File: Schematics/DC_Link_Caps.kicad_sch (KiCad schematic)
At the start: 15 parts

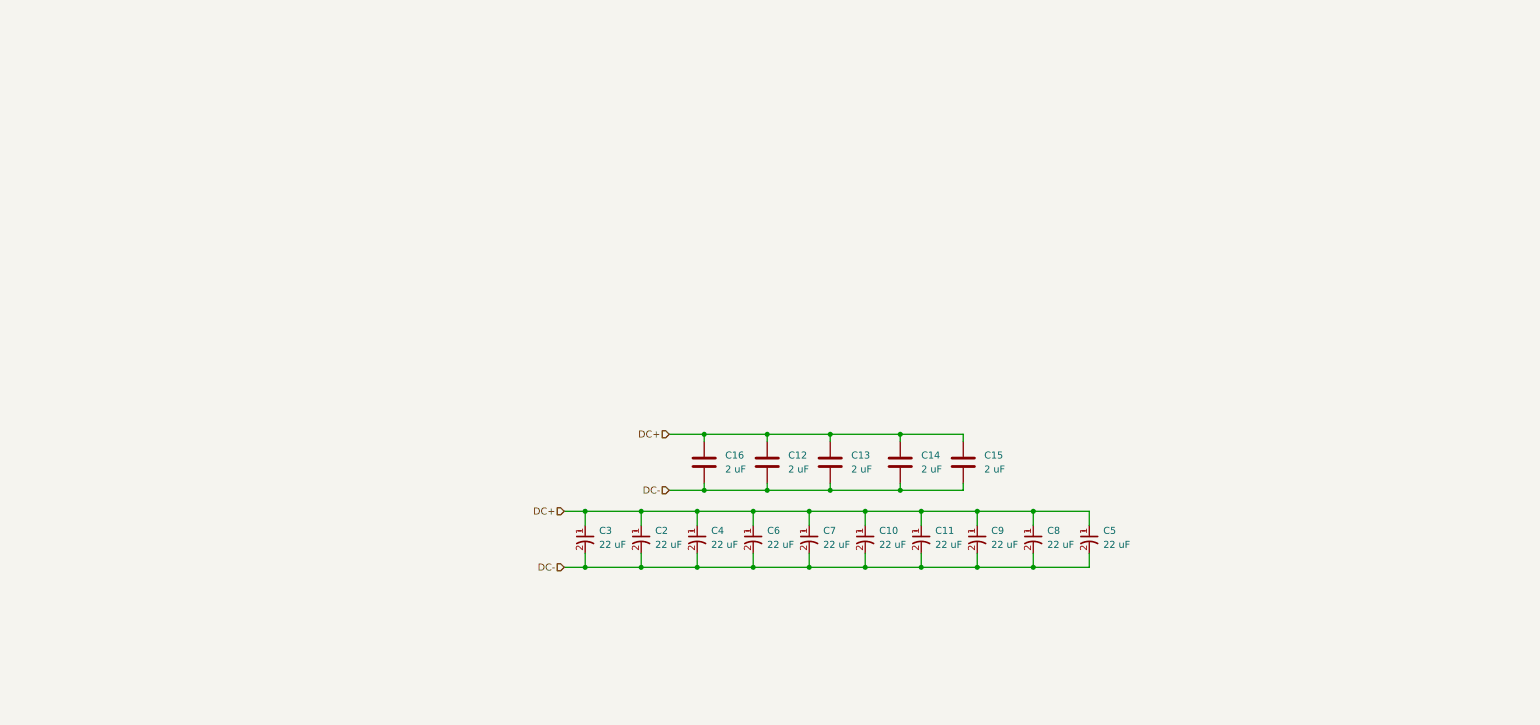
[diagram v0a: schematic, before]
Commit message: [SiC Inverter WIP]
- Deleted backup files
- changed symbol and footprint lib locations
- added text discription explaining the DC link sub sheet and emi  input
  filter subsheet
- Added Vin+,- Black and Red connector
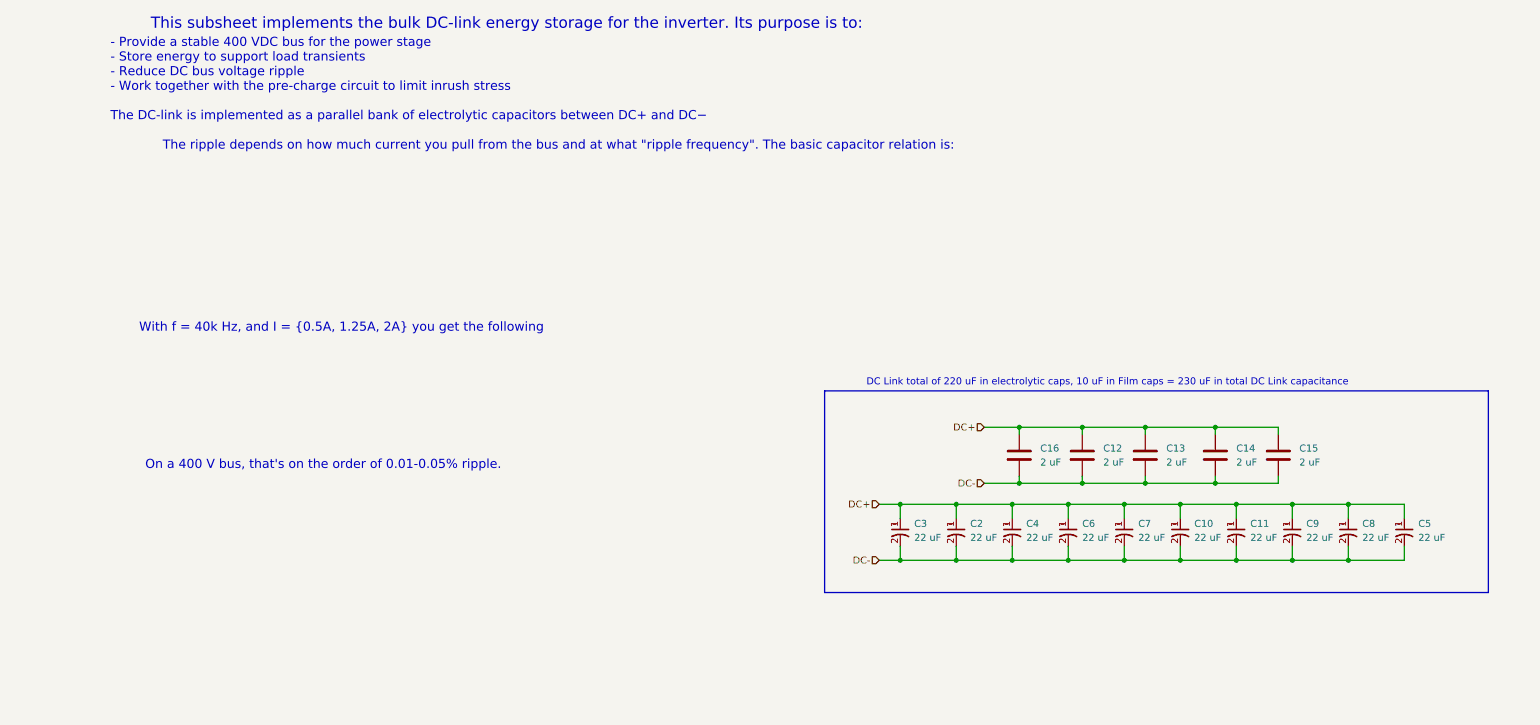
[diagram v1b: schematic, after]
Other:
- note added: "- Provide a stable 400 VDC bus for the power stage - Store energy to support load transients - Reduce DC bus voltage ripple - Work together with the pre‑charge circuit to limit inrush stress The DC‑link is implemented as a parallel bank of electrolytic capacitors between DC+ and DC−"
- note added: "DC Link total of 220 uF in electrolytic caps, 10 uF in Film caps = 230 uF in total DC Link capacitance"
- note added: "On a 400 V bus, that's on the order of 0.01-0.05% ripple."
- note added: "The ripple depends on how much current you pull from the bus and at what "ripple frequency". The basic capacitor relation is:"
- note added: "This subsheet implements the bulk DC‑link energy storage for the inverter. Its purpose is to:"
- note added: "With f = 40k Hz, and I = {0.5A, 1.25A, 2A} you get the following"
- moved on the sheet: C10, C11, C12, C13, C14, C15, C16, C2, C3, C4, C5, C6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

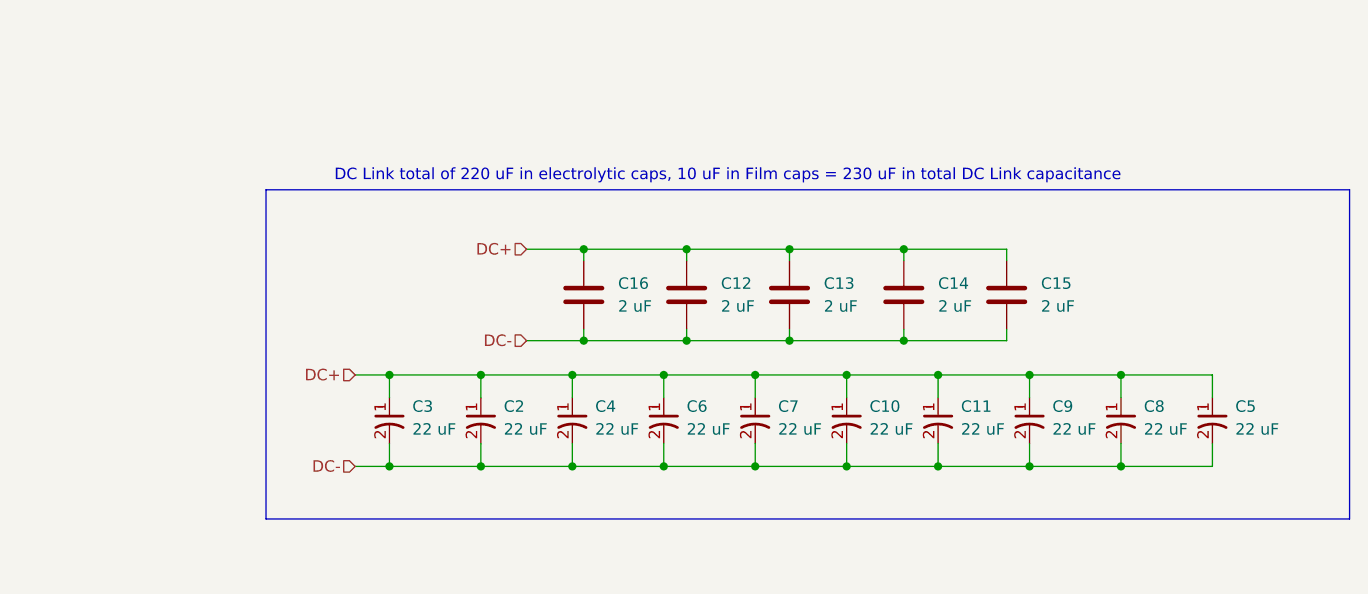
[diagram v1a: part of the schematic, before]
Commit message: [WIP - SIC Inverter]
- Added 3d models for 3 parts
- Added 3 new footprints for the 3 added parts
- Changed footprint 23AH8785 and 86 Black and Red
- Finished WIP with EMI, Input Protection, and Precharge
- Added datasheet
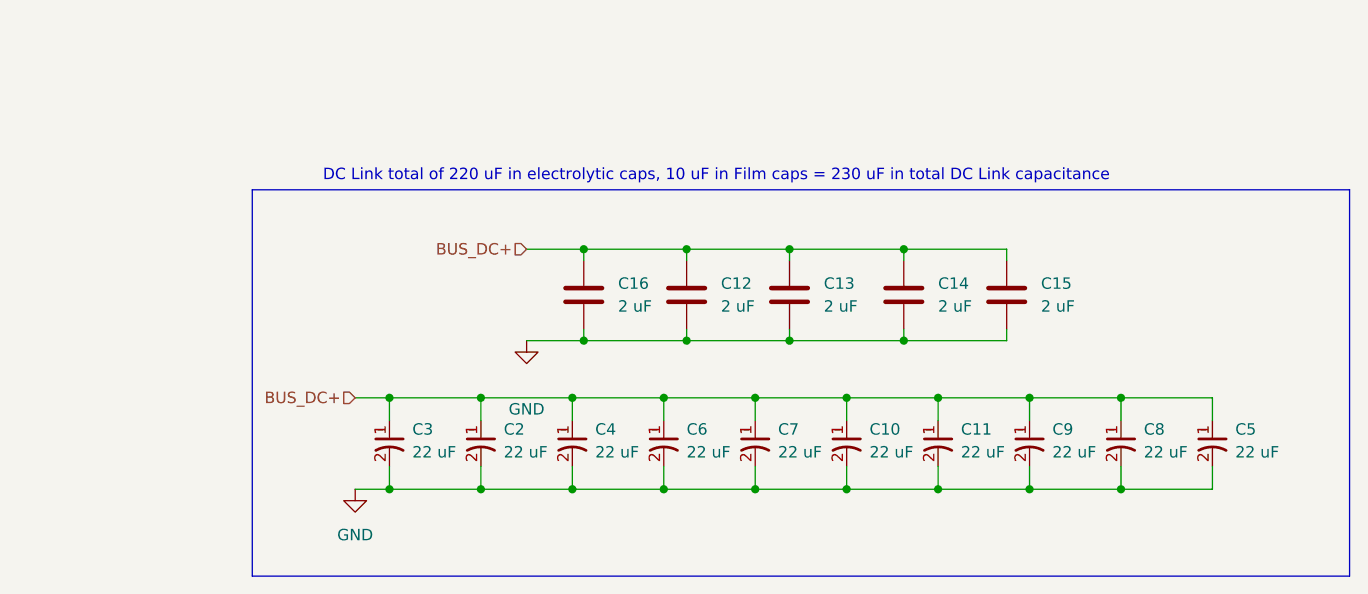
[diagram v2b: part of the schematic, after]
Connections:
- net DC+ renamed BUS_DC+
- net DC- renamed GND
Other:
- moved on the sheet: C10, C11, C2, C3, C4, C5, C6, C7, C8, C9

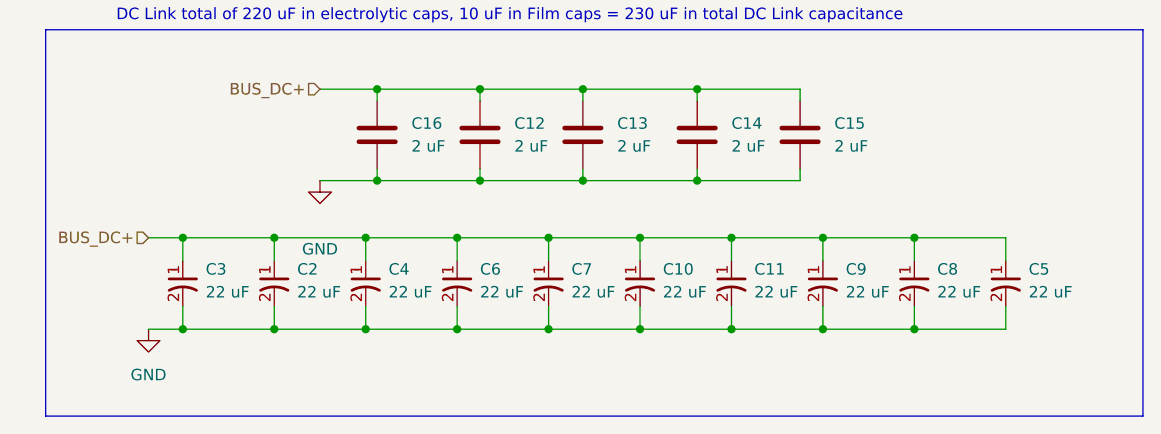
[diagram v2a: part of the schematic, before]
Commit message: [WIP Full Bridge Leg A High Side]
- Changed Footprint for Black and Red connectors to THP but no Pin
  number
- Changed DC Link cap sub sheet to have a cleaner look
- Change footprint in 1206 reister to head solder pads
- WIP Full Bridge Leg A High Side
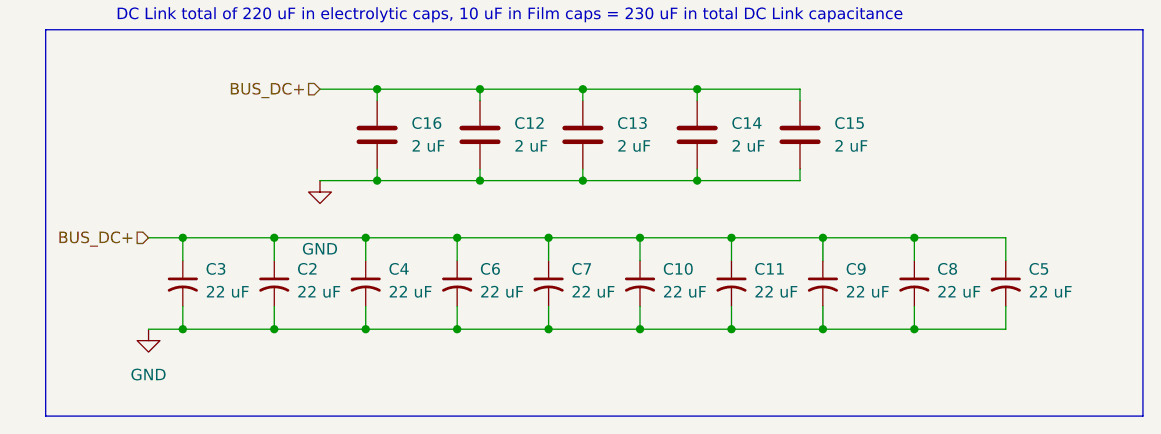
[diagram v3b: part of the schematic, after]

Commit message: Changing Text to Text Block
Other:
- note removed: "DC Link total of 220 uF in electrolytic caps, 10 uF in Film caps = 230 uF in total DC Link capacitance"
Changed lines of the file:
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@@
-		)
-	)
-	(text "DC Link total of 220 uF in electrolytic caps, 10 uF in Film caps = 230 uF in total DC Link capacitance"
-		(exclude_from_sim no)
-		(at 195.072 83.312 0)
-		(effects
-			(font
-				(size 1.27 1.27)
-			)
 		)
 	)
@@
 		)
 	)
+	(text_box "DC Link total of 220 uF in electrolytic caps, 10 uF in Film caps = 230 uF in total DC Link capacitance"
+		(exclude_from_sim no)
+		(at 143.51 81.534 0)
+		(size 105.918 3.048)
+		(margins 0.9525 0.9525 0.9525 0.9525)
+		(stroke
+			(width 0)
+			(type solid)
+		)
+		(fill
+			(type color)
+			(color 0 0 255 0.1)
+		)
+		(effects
+			(font
+				(size 1.27 1.27)
+			)
+			(justify left top)
+		)
+	)

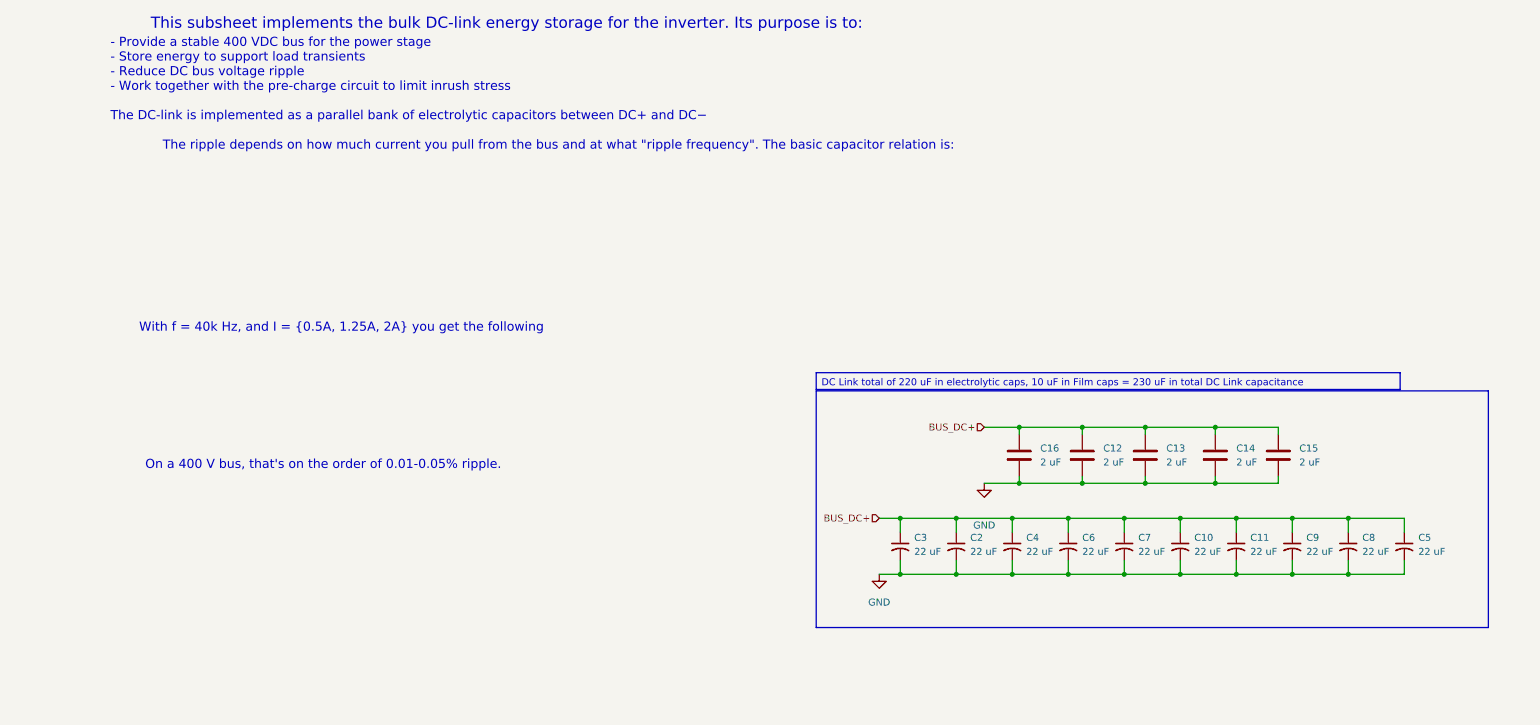
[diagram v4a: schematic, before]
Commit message: [WIP Single Phase SiC Inverter]
- Added molex 4 pin pcb connector for +15V power
- Added 3d model, symbol and footprint
- Added datasheet for molex connector
- Added Male and Female pcb - pcb connectors to all sub sheets
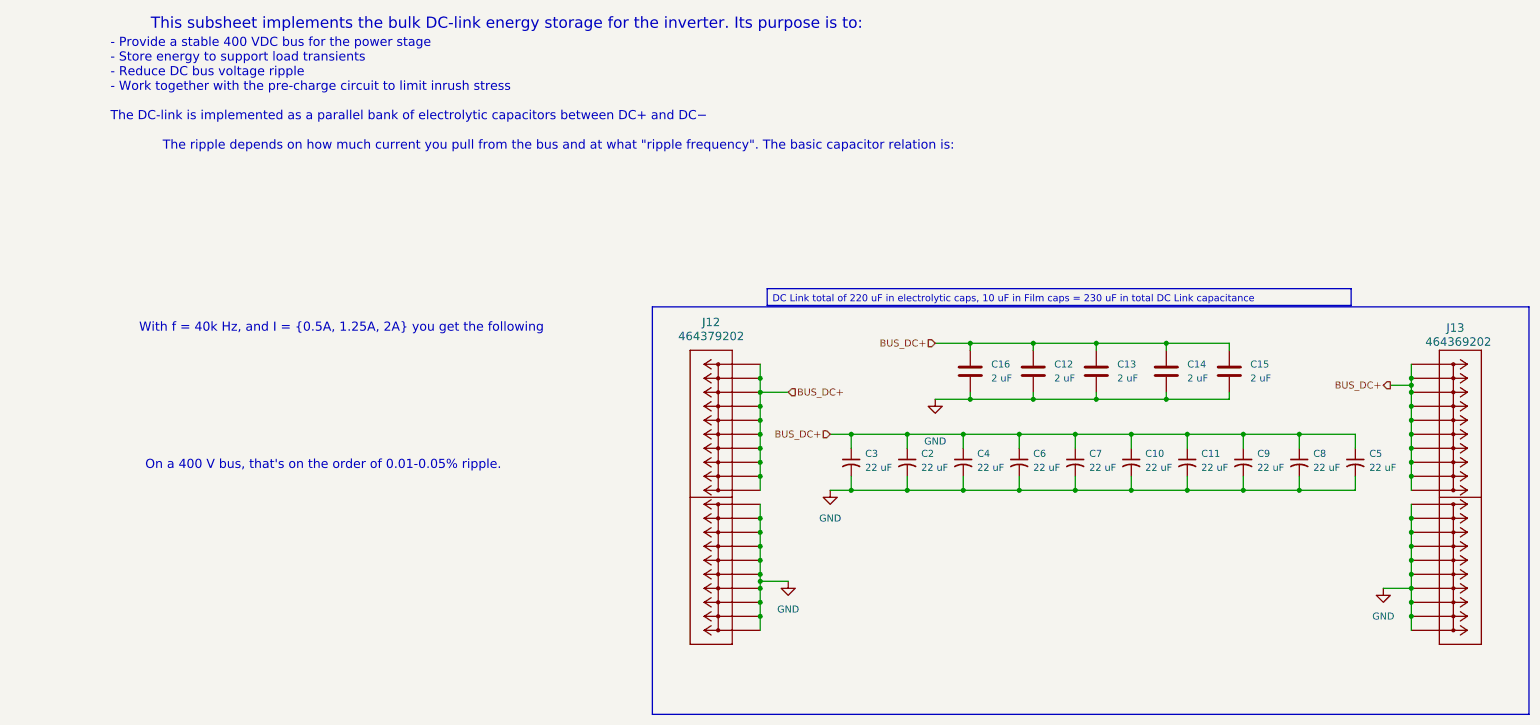
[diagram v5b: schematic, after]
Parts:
- added J12: 464379202, SiC_Inverter:46437-900_02, symbol SiC_Inverter:464379202
- added J13: 464369202, SiC_Inverter:46436-900_02, symbol SiC_Inverter:464369202
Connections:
- net BUS_DC+: now also J12.P2_1, J12.P2_10, J12.P2_2, J12.P2_3, J12.P2_4, J12.P2_5, J12.P2_6, J12.P2_7, J12.P2_8, J12.P2_9, J13.P1_1, J13.P1_10, J13.P1_2, J13.P1_3, J13.P1_4, J13.P1_5, J13.P1_6, J13.P1_7, J13.P1_8, J13.P1_9
- net GND: now also J12.P1_1, J12.P1_10, J12.P1_2, J12.P1_3, J12.P1_4, J12.P1_5, J12.P1_6, J12.P1_7, J12.P1_8, J12.P1_9, J13.P2_1, J13.P2_10, J13.P2_2, J13.P2_3, J13.P2_4, J13.P2_5, J13.P2_6, J13.P2_7, J13.P2_8, J13.P2_9
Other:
- moved on the sheet: C10, C11, C12, C13, C14, C15, C16, C2, C3, C4, C5, C6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
